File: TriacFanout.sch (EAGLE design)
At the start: 60 parts, among them IC1 MOC3020M, IC2 MOC3020M, IC3 MOC3020M, IC4 MOC3020M, IC5 MOC3020M, IC6 MOC3020M, IC7 MOC3020M, IC8 MOC3020M, IC9 74HC595N, T1 BTA12-600V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

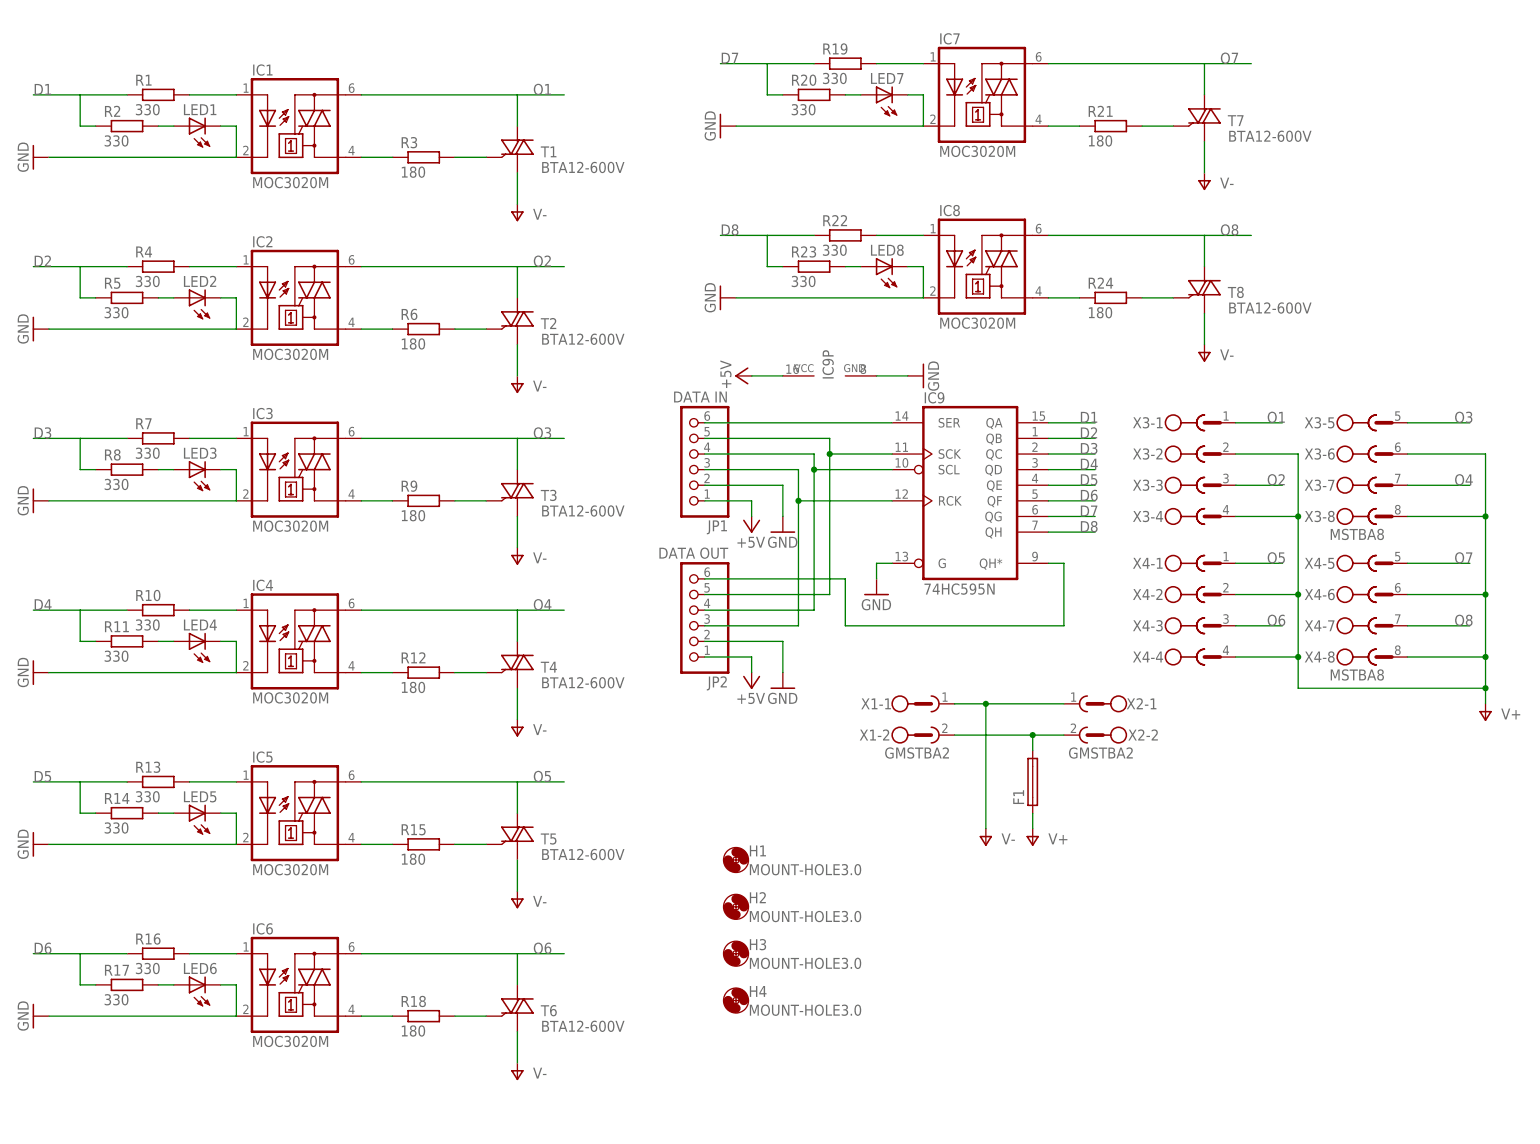
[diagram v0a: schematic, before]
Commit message: added triacfanout
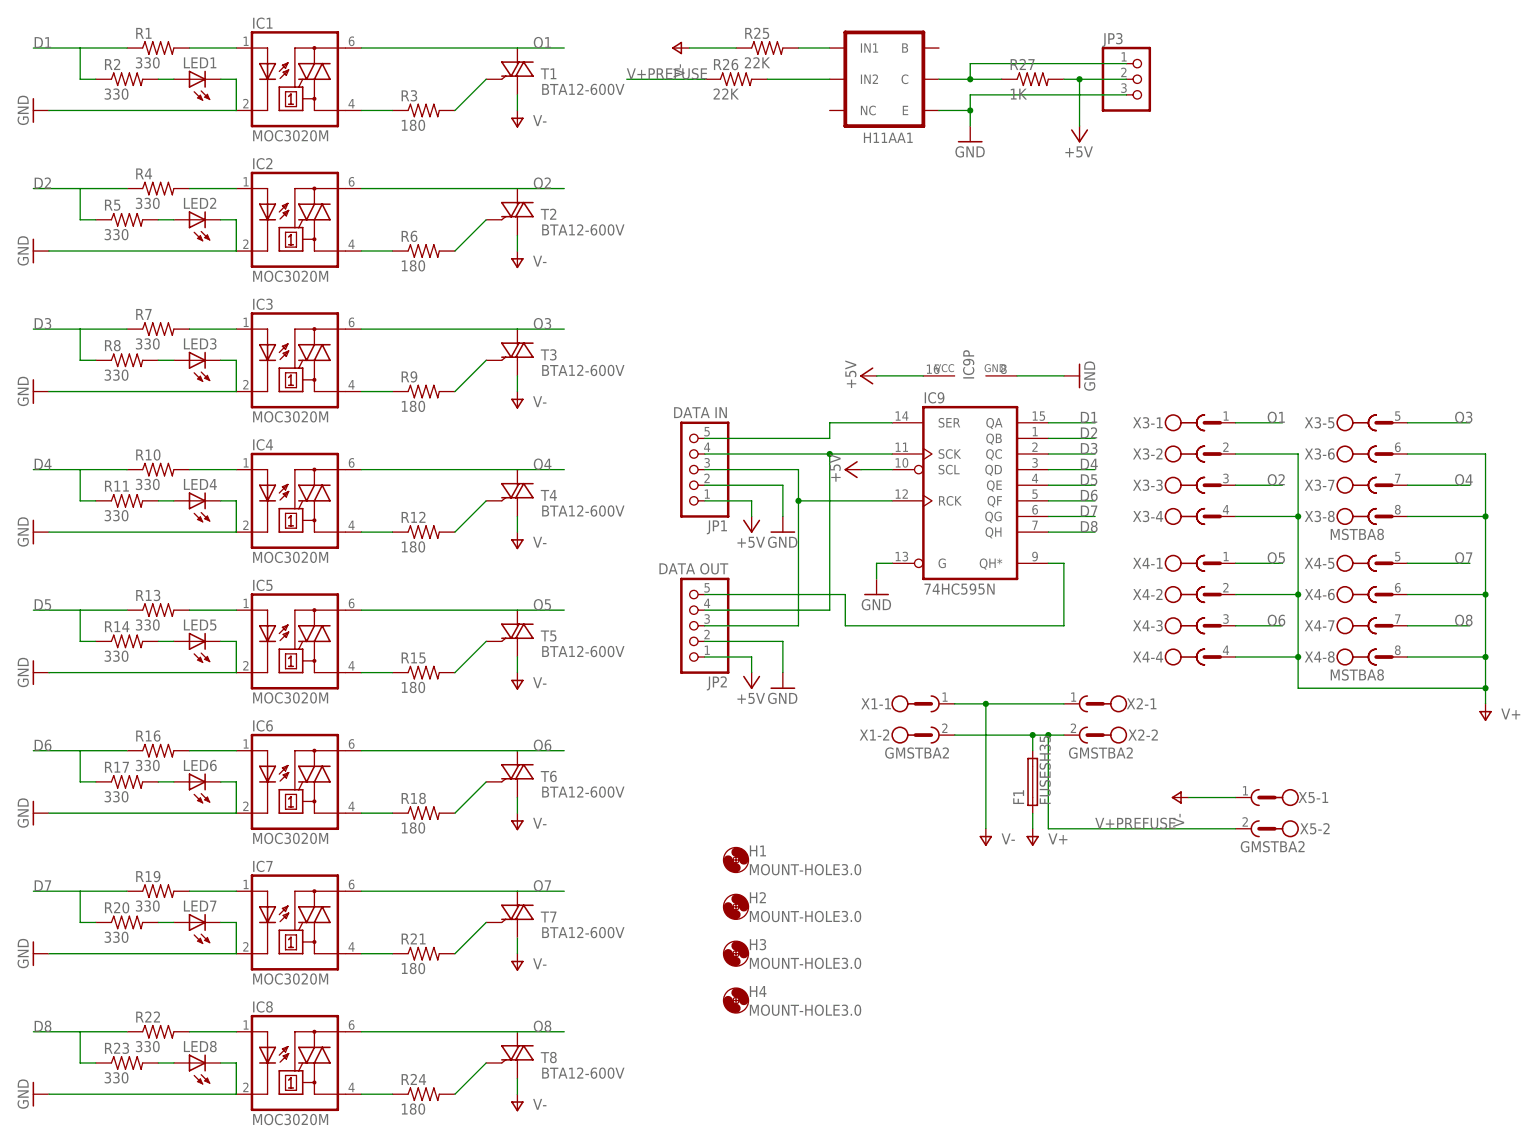
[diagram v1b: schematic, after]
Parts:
- added JP3: (no value), pinhead:PINHD-1X3
- added R25, R26: 22K, adafruit:R-US_0411/12
- added R27: 1K, adafruit:R-US_0207/10
- added U$1: H11AA1, boxysean:H11AA1
- added X5: GMSTBA2, con-phoenix-762:GMSTBA2
- F1: value (none) -> FUSESH35; device fuse:SH22,5 -> fuse:FUSESH35
- JP1, JP2: device pinhead:PINHD-1X6 -> pinhead:PINHD-1X5
- R1, R10, R11, R12, R13, R14, R15, R16, R17, R18, R19, R2, R20, R21, R22, R23, R24, R3, R4, R5, R6, R7, R8, R9: device resistor:R-EU_0204/7 -> adafruit:R-US_0207/10
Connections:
- net N$39 renamed LATCH
- removed net N$33: F1.2, X1-2.1, X2-2.1
- removed net N$35: IC9A.SER, JP1.6
- removed net N$36: IC9A.QH*, JP2.6
- removed net N$37: IC9A.SCK, JP1.5, JP2.5
- removed net N$38: IC9A.SCL, JP1.4, JP2.4
- new net CLOCK: IC9A.SCK, JP1.4, JP2.4
- new net DATA: IC9A.SER, JP1.5
- new net N$34: R25.2, U$1.IN1
- new net N$40: R26.2, U$1.IN2
- new net OVERFLOW: IC9A.QH*, JP2.5
- new net V+PREFUSE: F1.2, R26.1, X1-2.1, X2-2.1, X5-2.1
- new net ZEROCROSS: JP3.1, R27.1, U$1.C
- net +5V: now also IC9A.SCL, JP3.2, R27.2
- net GND: now also JP3.3, U$1.E
- net V-: now also R25.1, X5-1.1
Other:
- moved on the sheet: IC1, IC2, IC3, IC4, IC5, IC6, IC7, IC8, IC9P, LED1, LED2, LED3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
